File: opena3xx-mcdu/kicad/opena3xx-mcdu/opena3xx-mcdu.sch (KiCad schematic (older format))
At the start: 49 parts, among them J1 Conn_02x01, J2 Conn_02x01, J3 Conn_02x01, J4 Conn_02x01, J5 Raspberry_Pi_Zero, SW1 SW_MEC_5E, U1 MCP23017_SO, U2 MCP23017_SO, U3 MCP23017_SO, U4 MCP23017_SO, U5 MCP23017_SO, U6 MCP23017_SO, U7 MCP23017_SO, U8 MCP23017_SO

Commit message: WIP Schematic & PCB for the MCDU Added custom Kicad Packages for the Tactile Switchs (LED EMBEDDED)
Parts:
- removed BUS0, BUS1, BUS2, BUS3, BUS4, BUS5, BUS6, BUS7: Conn_02x08_Counter_Clockwise, Connector_PinHeader_2.54mm:PinHeader_2x08_P2.54mm_Vertical, symbol Connector_Generic:Conn_02x08_Counter_Clockwise
- removed C6, C7, C8: 100n, Capacitor_SMD:C_1206_3216Metric_Pad1.33x1.80mm_HandSolder, symbol Device:C_Small
- removed R10, R11, R12: 10k, Resistor_SMD:R_1206_3216Metric_Pad1.30x1.75mm_HandSolder, symbol Device:R_Small
- removed U6, U7, U8: MCP23017_SO, Package_SO:SOIC-28W_7.5x17.9mm_P1.27mm, symbol Interface_Expansion:MCP23017_SO
- added SW100, SW? (x11): TLL-6A, openaa3xx:TACTILE_LED_TH, symbol opena3xx-kicad:TLL-6A
- SW1: footprint Button_Switch_THT:SW_Tactile_Straight_KSL0Axx1LFTR -> Button_Switch_THT:SW_TH_Tactile_Omron_B3F-10xx
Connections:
- net labels added: SIGNAL_LED
- net labels removed: BUS5-0, BUS5-1, BUS5-10, BUS5-11, BUS5-12, BUS5-13, BUS5-14, BUS5-15, BUS5-2, BUS5-3, BUS5-4, BUS5-5, BUS5-6, BUS5-7, BUS5-8, BUS5-9, BUS6-0, BUS6-1, BUS6-10, BUS6-11, BUS6-12, BUS6-13, BUS6-14, BUS6-15, BUS6-2, BUS6-3, BUS6-4, BUS6-5, BUS6-6, BUS6-7, BUS6-8, BUS6-9, BUS7-0, BUS7-1, BUS7-10, BUS7-11, BUS7-12, BUS7-13, BUS7-14, BUS7-15, BUS7-2, BUS7-3, BUS7-4, BUS7-5, BUS7-6, BUS7-7, BUS7-8, BUS7-9, INT_BUS_5, INT_BUS_6, INT_BUS_7, MESSAGING_LED
- wire segments 486 -> 258
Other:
- moved on the sheet: C1, C2, C3, C4, C5, D1, D2, D3, D4, J1, J2, J3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

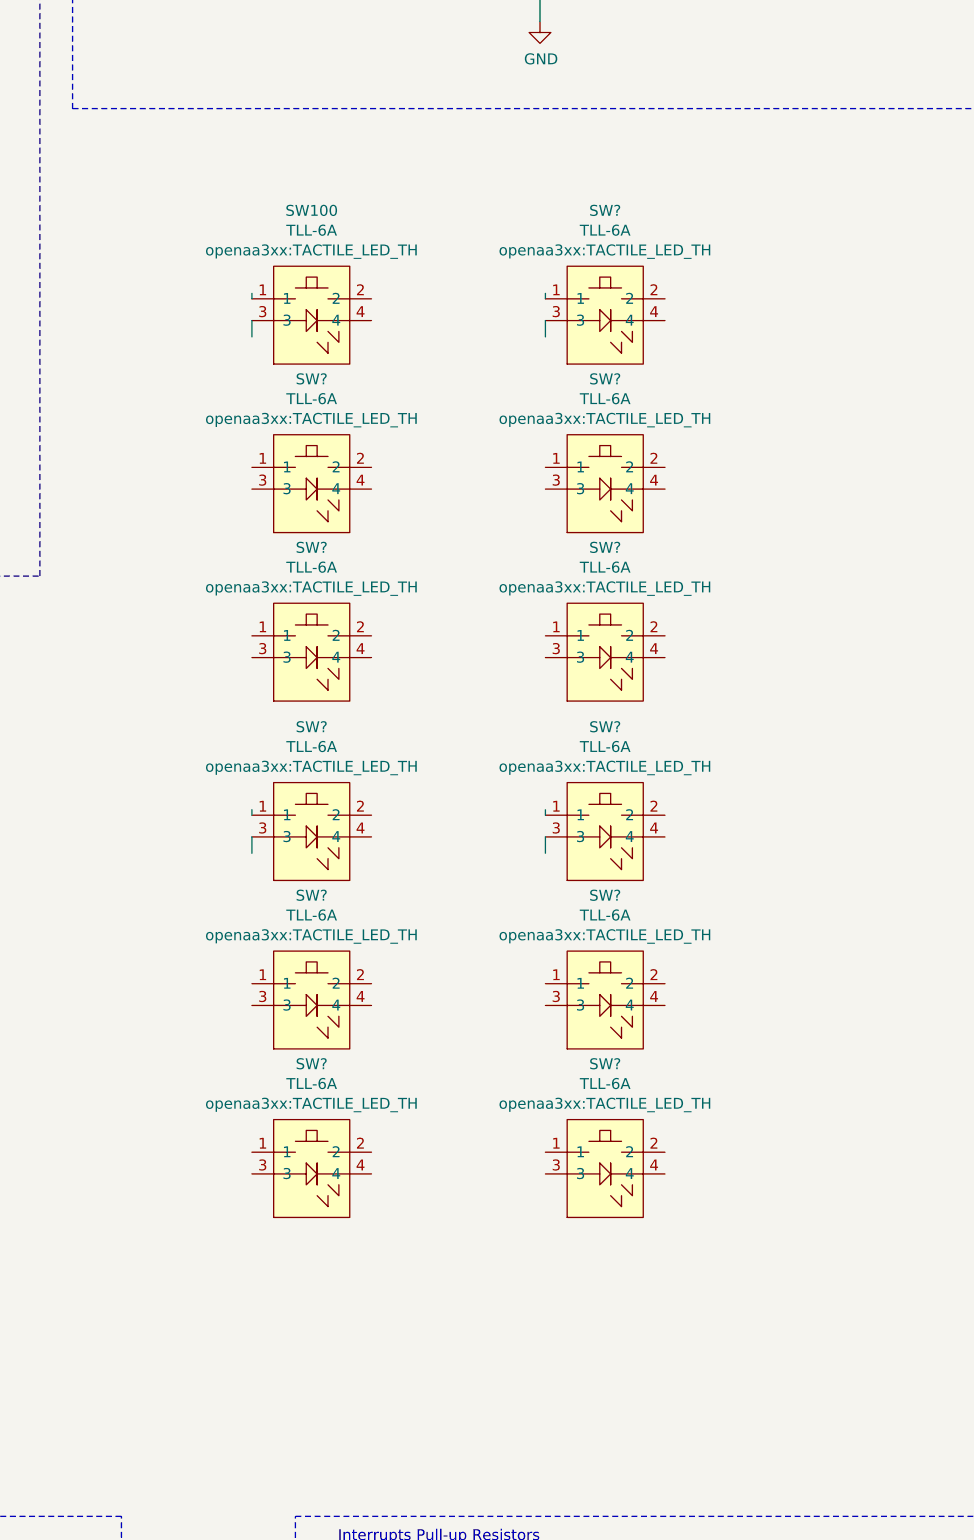
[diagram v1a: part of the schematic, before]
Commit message: Schematic Updates - MCDU
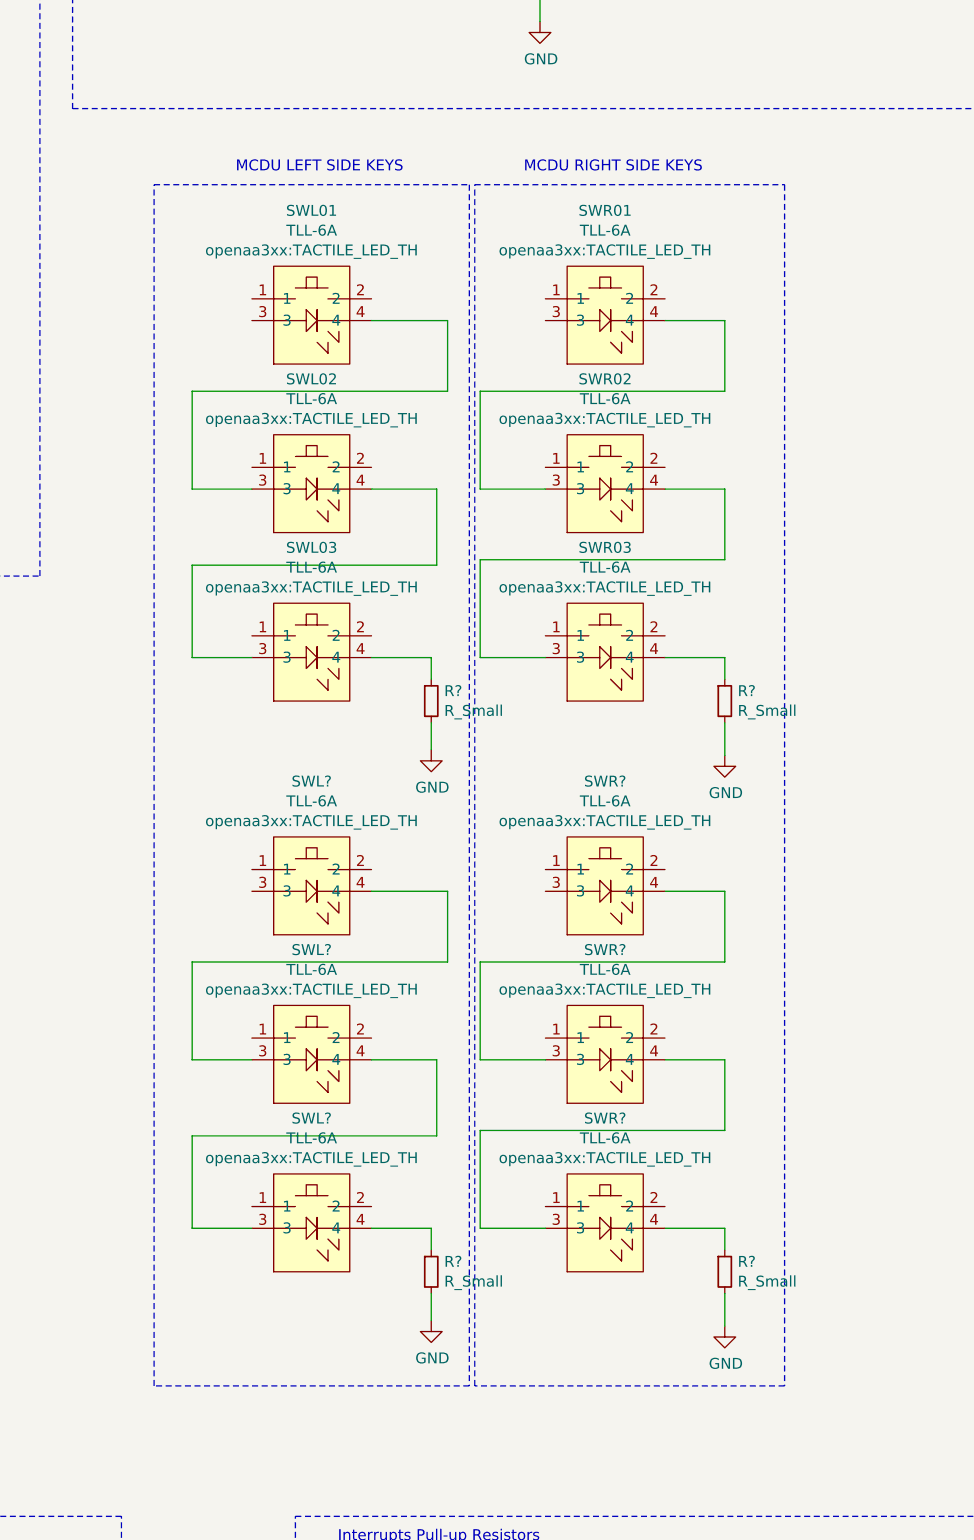
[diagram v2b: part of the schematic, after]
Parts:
- removed SW? (x6): TLL-6A, openaa3xx:TACTILE_LED_TH, symbol opena3xx-kicad:TLL-6A
- added R? (x4): R_Small, symbol Device:R_Small
- added SWL? (x3), SWR? (x3): TLL-6A, openaa3xx:TACTILE_LED_TH, symbol opena3xx-kicad:TLL-6A
- gave numbers to parts that had none: 5
- renumbered SW100 to SWL01
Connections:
- net GND: now also R?.2, R?.2, R?.2, R?.2
- net at SWL01.4: now also SWL02.3
- net at SWL02.4: now also SWL03.3
- net at SWL03.4: now also R?.1
- net at SWR01.4: now also SWR02.3
- net at SWR02.4: now also SWR03.3
- net at SWR03.4: now also R?.1
- new net: SWL?.3, SWL?.4 (x2)
- new net: R?.1, SWL?.4
- new net: SWR?.3, SWR?.4 (x2)
- new net: R?.1, SWR?.4
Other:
- note added: "MCDU LEFT SIDE KEYS\n"
- note added: "MCDU RIGHT SIDE KEYS\n"
